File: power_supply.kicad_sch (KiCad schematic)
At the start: 26 parts

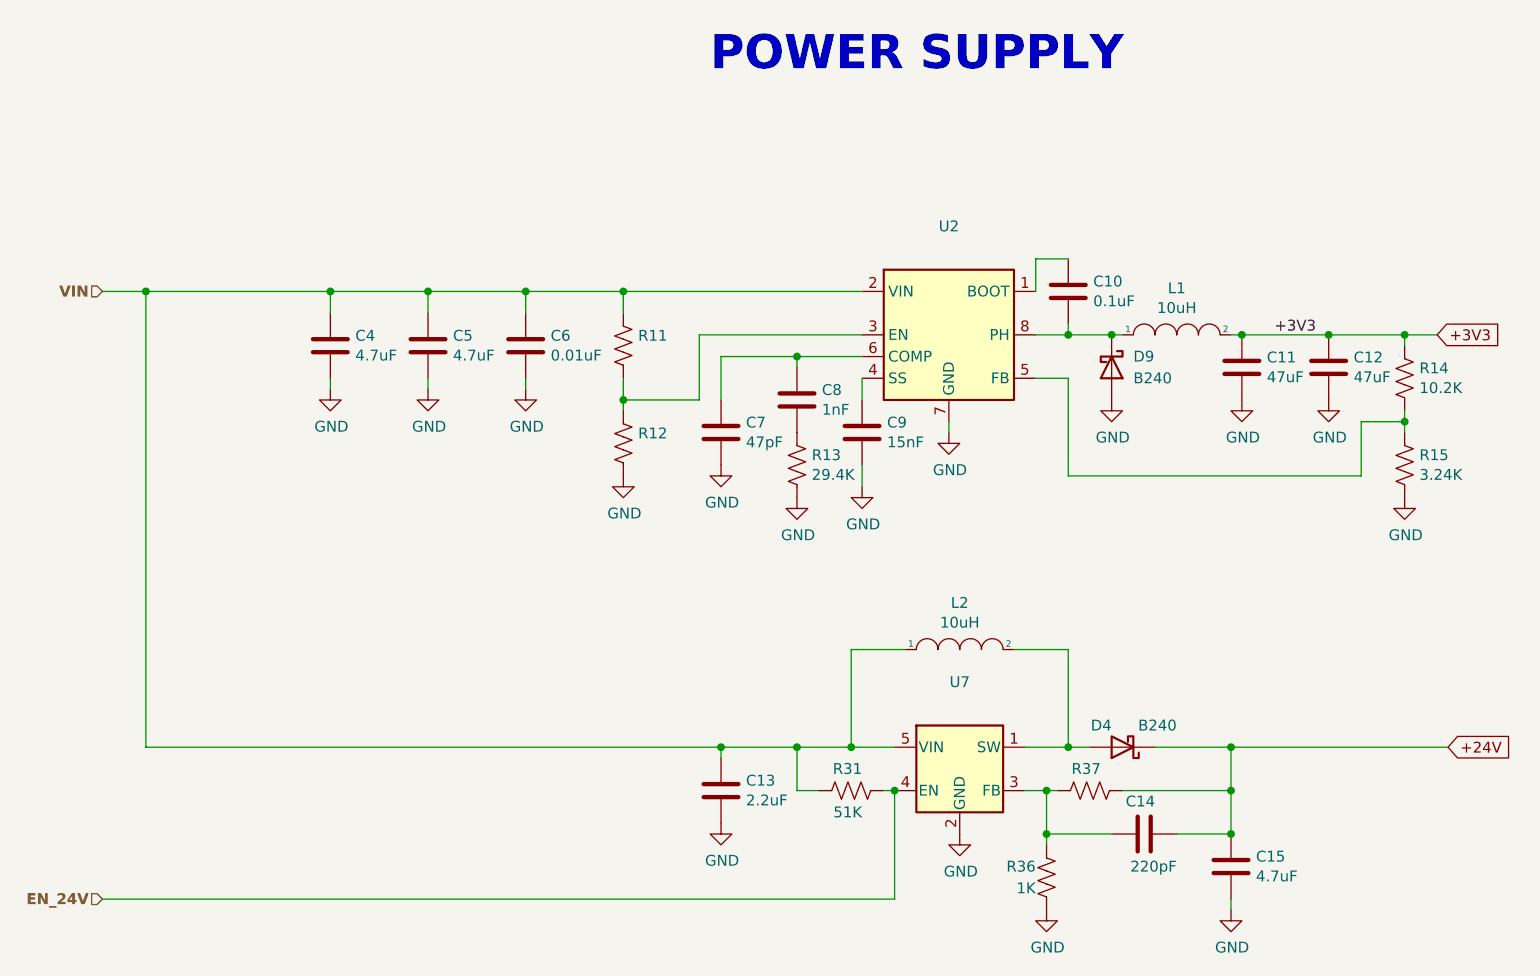
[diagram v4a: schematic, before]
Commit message: Replaced relays with smd versions.
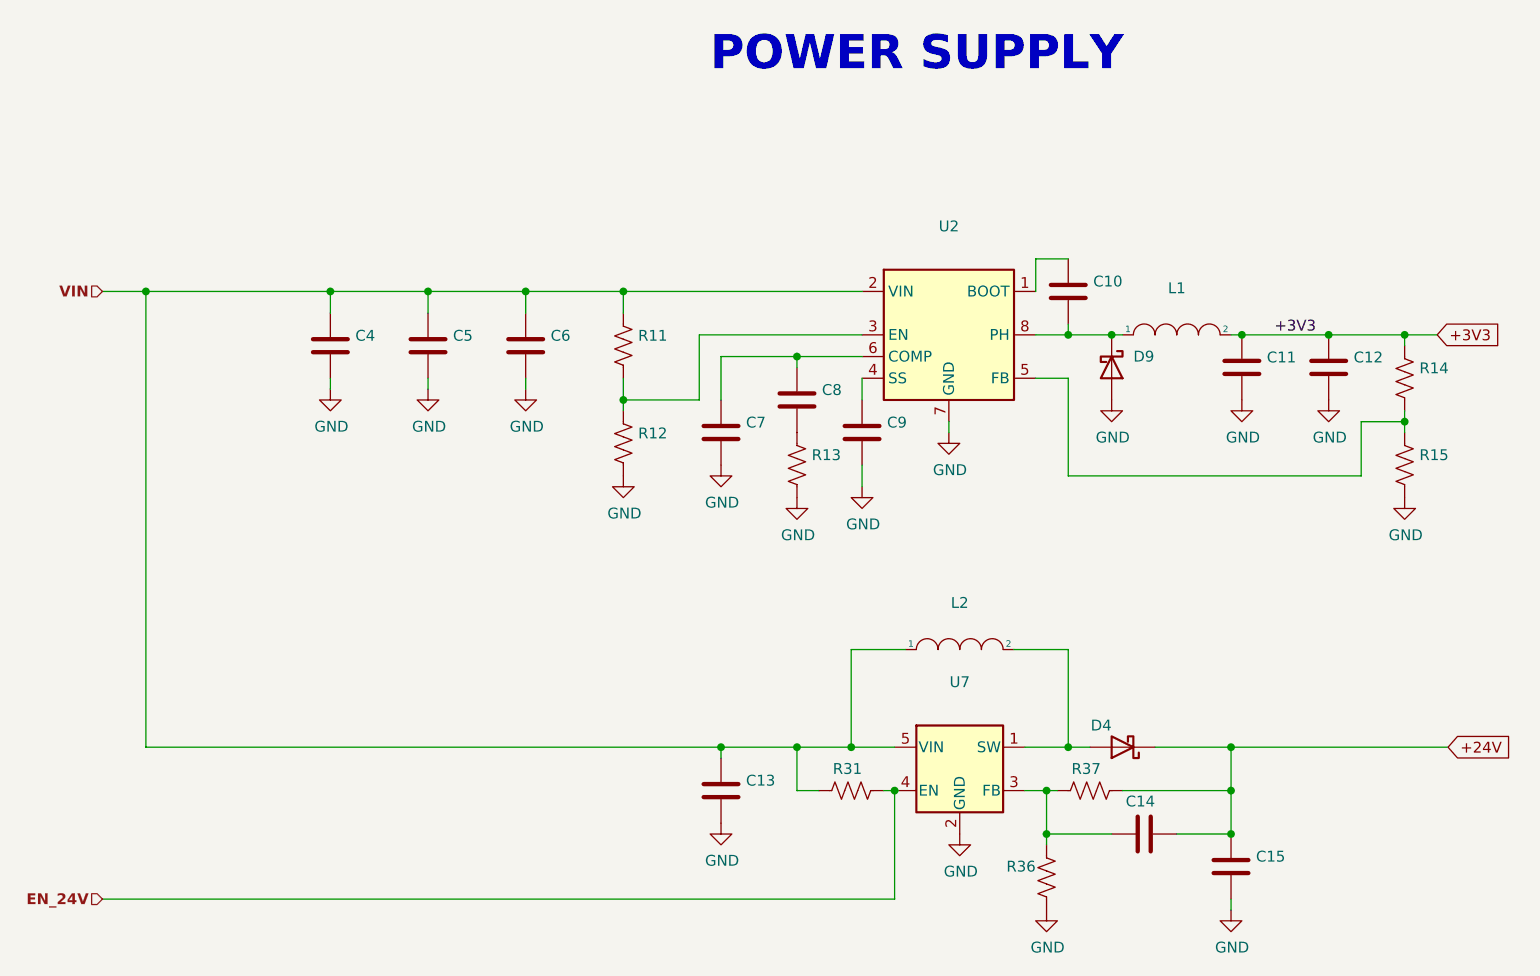
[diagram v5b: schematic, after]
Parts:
- C10: value 0.1uF -> (none); footprint Capacitor_SMD:C_0805_2012Metric -> (none)
- C11, C12: value 47uF -> (none); footprint Capacitor_SMD:C_0805_2012Metric -> (none)
- C13: value 2.2uF -> (none); footprint Capacitor_SMD:C_0805_2012Metric -> (none)
- C14: value 220pF -> (none); footprint Capacitor_SMD:C_0805_2012Metric -> (none)
- C15, C4, C5: value 4.7uF -> (none); footprint Capacitor_SMD:C_0805_2012Metric -> (none)
- C6: value 0.01uF -> (none); footprint Capacitor_SMD:C_0805_2012Metric -> (none)
- C7: value 47pF -> (none); footprint Capacitor_SMD:C_0805_2012Metric -> (none)
- C8: value 1nF -> (none); footprint Capacitor_SMD:C_0805_2012Metric -> (none)
- C9: value 15nF -> (none); footprint Capacitor_SMD:C_0805_2012Metric -> (none)
- D4, D9: value B240 -> (none); footprint Diode_SMD:D_SMB -> (none)
- L1, L2: value 10uH -> (none); footprint Inductor_SMD:L_Taiyo-Yuden_NR-50xx -> (none)
- R11: footprint Resistor_SMD:R_0805_2012Metric -> (none)
- R13: value 29.4K -> (none); footprint Resistor_SMD:R_0805_2012Metric -> (none)
- R14: value 10.2K -> (none); footprint Resistor_SMD:R_0805_2012Metric -> (none)
- R15: value 3.24K -> (none); footprint Resistor_SMD:R_0805_2012Metric -> (none)
- R31: value 51K -> (none); footprint Resistor_SMD:R_0805_2012Metric -> (none)
- R36: value 1K -> (none); footprint Resistor_SMD:R_0805_2012Metric -> (none)
- U2: footprint Package_SO:SOIC-8_3.9x4.9mm_P1.27mm -> (none)
- U7: footprint Package_TO_SOT_SMD:SOT-23-5 -> (none)
